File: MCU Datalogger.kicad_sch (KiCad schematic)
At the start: 25 parts, among them U1 24LC1025, U2 24LC1025, U3 DS1337S_, U4 ATMEGA328P-AU, Y1 16 MHz, Y2 32.768 KHz

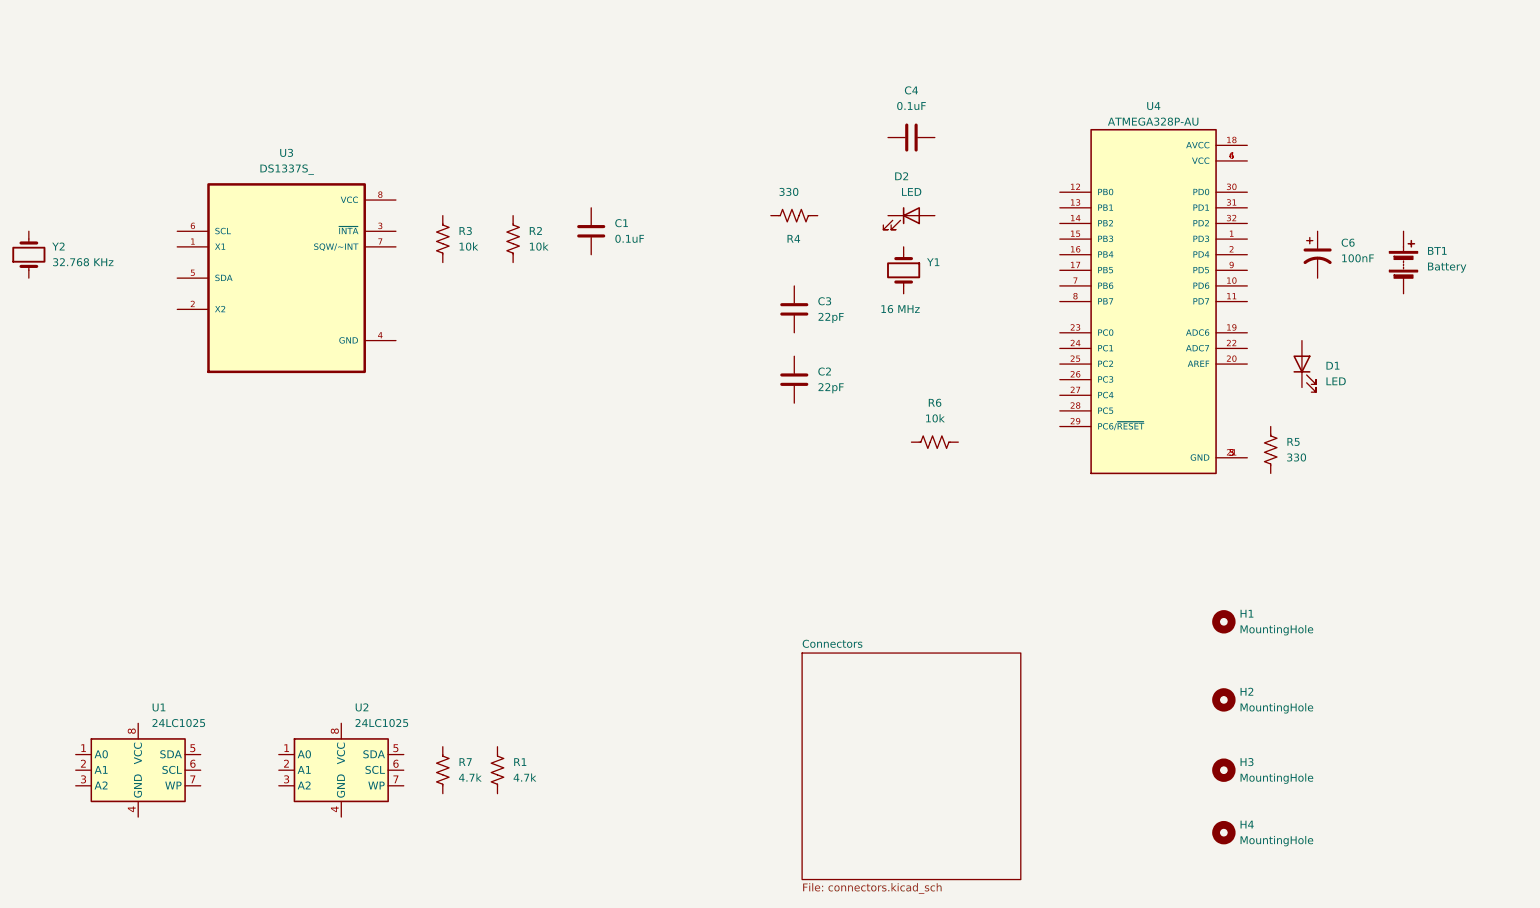
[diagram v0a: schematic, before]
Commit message: Completed wiring and ERC. Fixed some issues.
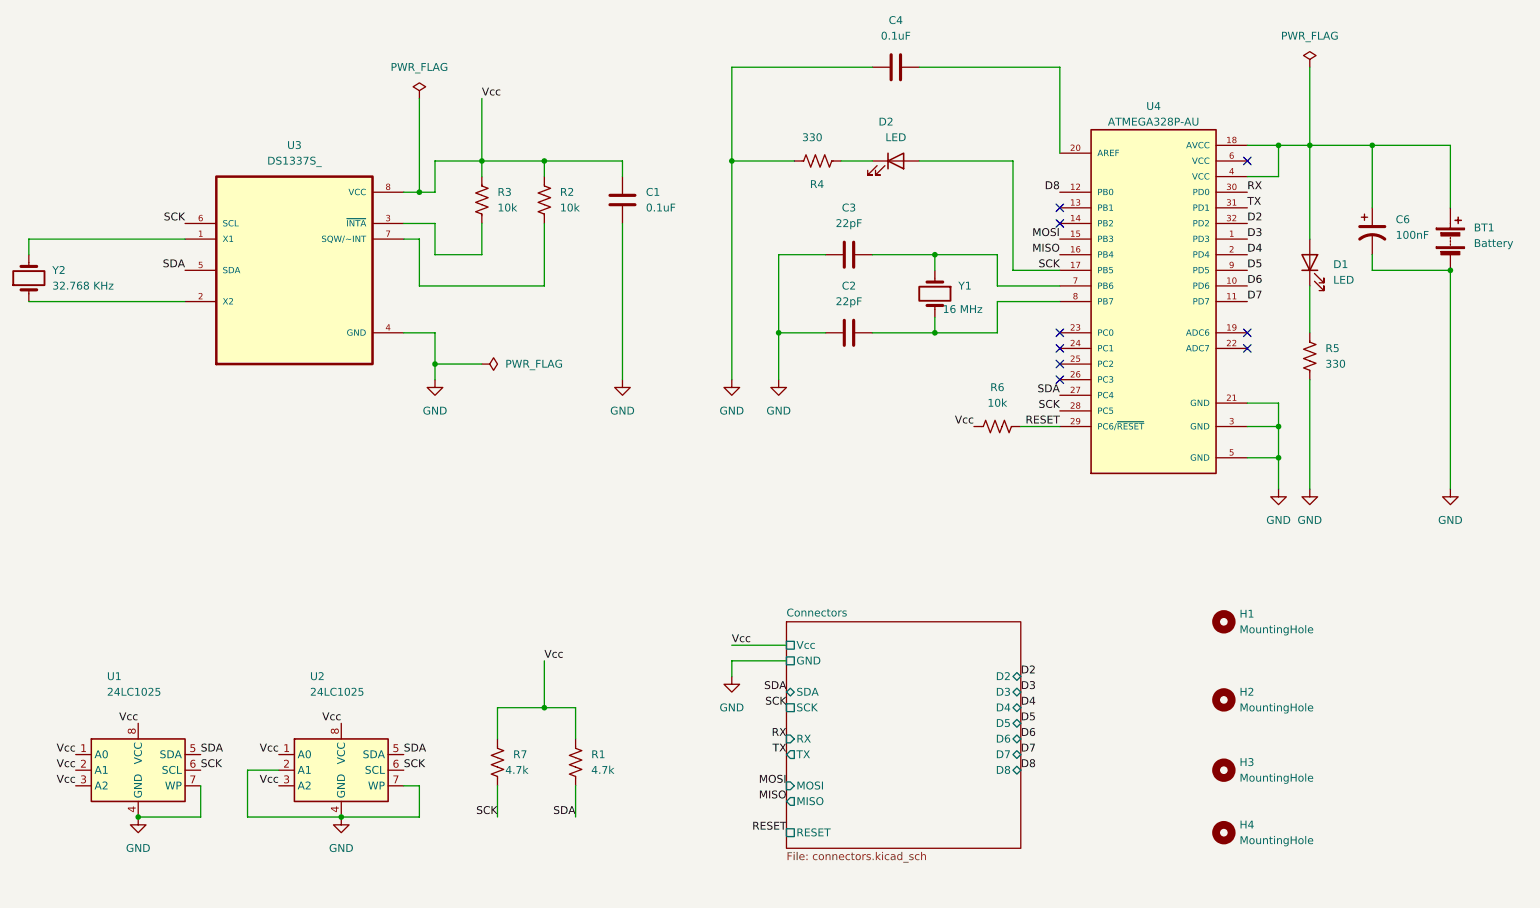
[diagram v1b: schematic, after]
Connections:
- net at BT1.1 (+): now also C6.1, D1.2 (A), U4.18 (AVCC), U4.4 (VCC)
- net GND: now reaches BT1.2 (-)
- net GND: now also C1.2, C2.1, C3.1, C4.1, C6.2, R4.2, R5.2, U1.4 (GND), U1.7 (WP), U2.2 (A1), U2.4 (GND), U2.7 (WP), U3.4 (GND), U4.21 (GND), U4.3 (GND), U4.5 (GND)
- net at C2.2: now also U4.8 (PB7), Y1.2
- net at Y1.1: now also C3.2, U4.7 (PB6)
- net SCK: now reaches R7.1
- net SCK: now also D2.2 (A), U1.6 (SCL), U2.6 (SCL), U3.6 (SCL), U4.17 (PB5), U4.28 (PC5)
- net Vcc: now reaches R7.2
- net Vcc: now also C1.1, R1.1, R2.1, R3.1, R6.1, U1.1 (A0), U1.2 (A1), U1.3 (A2), U1.8 (VCC), U2.1 (A0), U2.3 (A2), U2.8 (VCC), U3.8 (VCC)
- net at R4.1: now also D2.1 (K)
- net D3: now reaches U4.1 (PD3)
- net D6: now reaches U4.10 (PD6)
- net D7: now reaches U4.11 (PD7)
- net D8: now reaches U4.12 (PB0)
- net MOSI: now reaches U4.15 (PB3)
- net MISO: now reaches U4.16 (PB4)
- net D4: now reaches U4.2 (PD4)
- net at U4.20 (AREF): now also C4.2
- net SDA: now reaches U4.27 (PC4)
- net SDA: now also R1.2, U1.5 (SDA), U2.5 (SDA), U3.5 (SDA)
- net RESET: now reaches U4.29 (PC6/~{RESET})
- net RESET: now also R6.2
- net RX: now reaches U4.30 (PD0)
- net TX: now reaches U4.31 (PD1)
- net D2: now reaches U4.32 (PD2)
- net at U4.6 (VCC): no longer U4.4 (VCC)
- net D5: now reaches U4.9 (PD5)
- net at U3.1 (X1): now also Y2.2
- net at U3.2 (X2): now also Y2.1
- net at U3.3 (~{INTA}): now also R3.2
- net at U3.7 (SQW/~INT): now also R2.2
- net at R5.1: now also D1.1 (K)
- no-connect marks 0 -> 9
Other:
- sheet Connectors ports: added D2, D3, D4, D5, D6, D7, D8, GND, MISO, MOSI, RESET, RX, SCK, SDA, TX, Vcc; removed none
- moved on the sheet: BT1, C1, C2, C3, C4, C6, D1, D2, R1, R2, R3, R4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
